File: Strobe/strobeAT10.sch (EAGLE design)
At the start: 11 parts, among them Q2 BC848, U2 ATTINY10-TS8R

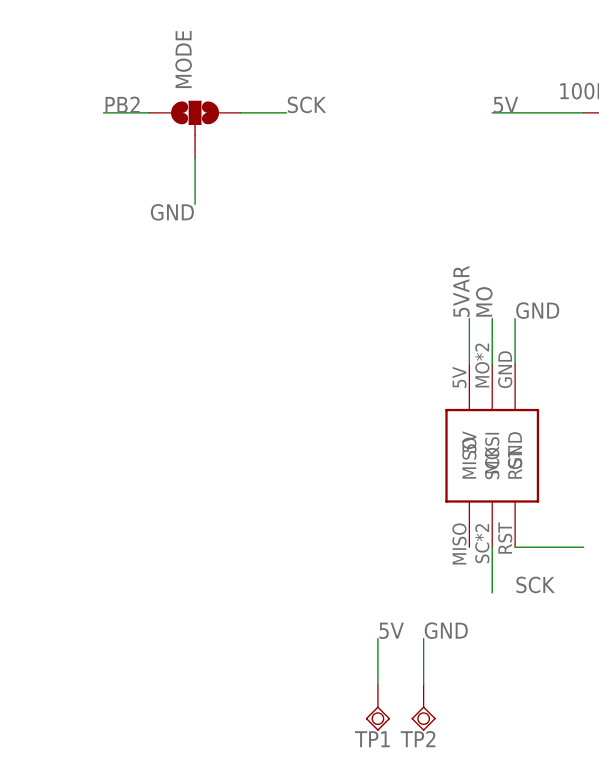
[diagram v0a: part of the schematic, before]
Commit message: PCB updates (jumper distance) and a new RGB mini board
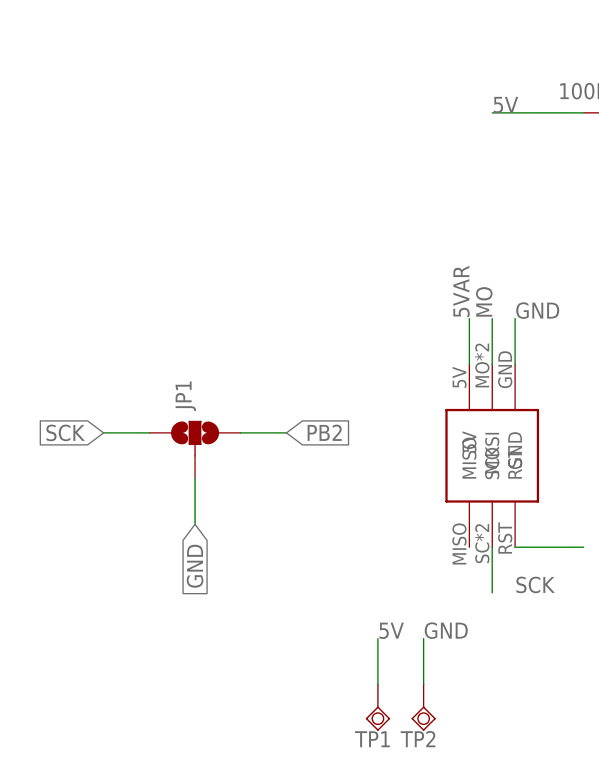
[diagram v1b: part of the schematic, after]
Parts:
- removed MODE: JUMPER-SMT_3_NO_SILK, SparkFun-Jumpers:JUMPER-SMT_3_NO_SILK
- added JP1: JUMPER-SMT_3_NO_SILK, SparkFun-Jumpers:JUMPER-SMT_3_NO_SILK
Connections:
- net GND: now also JP1.2; no longer MODE.2
- net PB2: now also JP1.3; no longer MODE.1
- net SCK: now also JP1.1; no longer MODE.3
